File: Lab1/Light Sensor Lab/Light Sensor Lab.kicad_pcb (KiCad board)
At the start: 2 copper layers, 19.3 x 19.8 mm, 9 parts, among them J1 Conn_01x03, U1 LMC6482

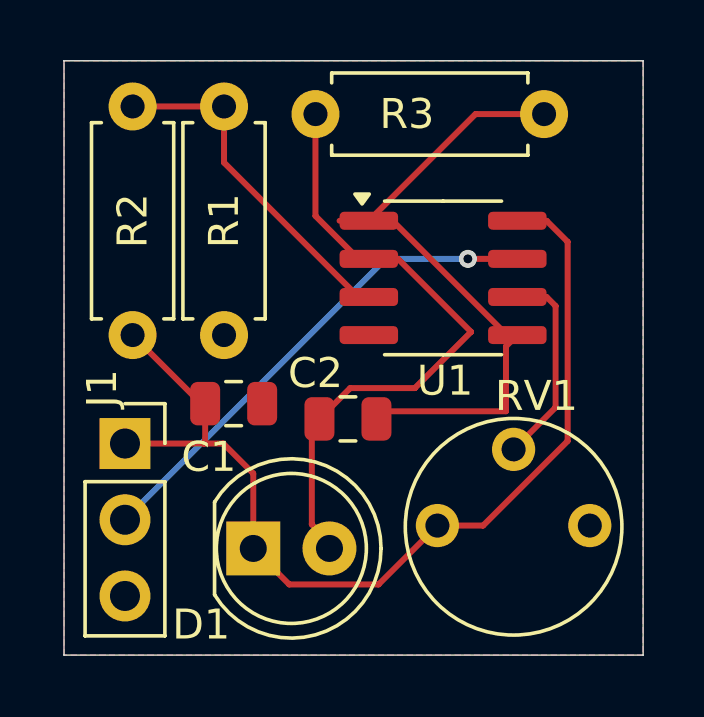
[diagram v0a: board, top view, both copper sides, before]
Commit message: small trace tweeks
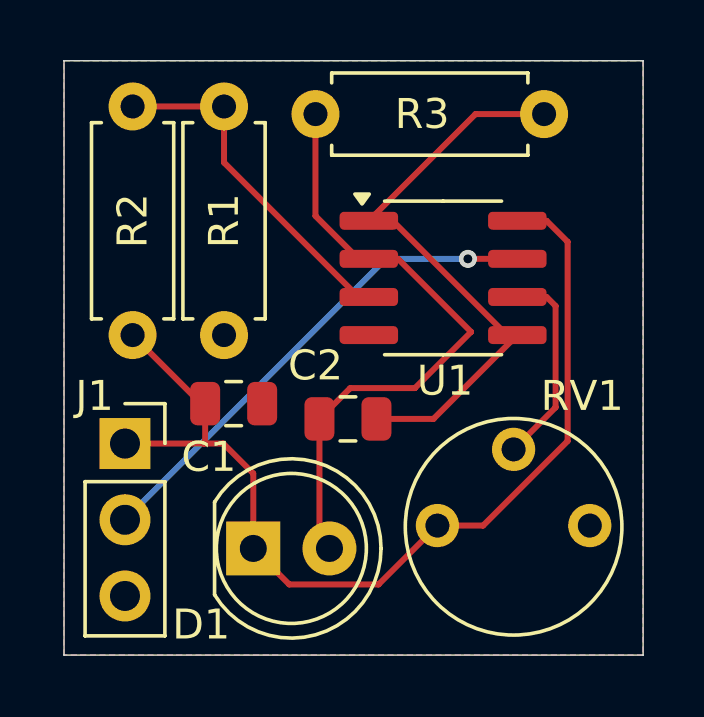
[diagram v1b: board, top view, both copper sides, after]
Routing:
- net Net-(U1B-+): track 22.1 -> 19.7 mm
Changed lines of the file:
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@@
 		(tags "capacitor")
 		(property "Reference" "C2"
-			(at -1.082 -1.524 0)
+			(at -1.082 -1.778 0)
 			(layer "F.SilkS")
 			(effects
@@
 		(tags "Resistor Axial_DIN0207 series Axial Horizontal pin pitch 7.62mm 0.25W = 1/4W length 6.3mm diameter 2.5mm")
 		(property "Reference" "R3"
-			(at 3.048 0 0)
+			(at 3.556 0 0)
 			(layer "F.SilkS")
 			(effects
@@
 		(tags "Through hole socket strip THT 1x03 2.54mm single row")
 		(property "Reference" "J1"
-			(at -0.762 -1.838 90)
+			(at -1.016 -1.584 180)
 			(layer "F.SilkS")
 			(effects
@@
 		(tags "Potentiometer vertical Vishay T7-YA Single")
 		(property "Reference" "RV1"
-			(at 4.318 -1.778 180)
+			(at 4.318 -0.254 180)
 			(layer "F.SilkS")
 			(effects
@@
 		(layer "Edge.Cuts")
 	)
+	(dimension
+		(type orthogonal)
+		(layer "F.Cu")
+		(pts
+			(xy 158.496 78.74) (xy 139.192 78.74)
+		)
+		(height -3.048)
+		(orientation 0)
+		(format
+			(prefix "")
+			(suffix "")
+			(units 3)
+			(units_format 0)
+			(precision 4)
+			(suppress_zeroes yes)
+		)
+		(style
+			(thickness 0.2)
+			(arrow_length 1.27)
+			(text_position_mode 0)
+			(arrow_direction outward)
+			(extension_height 0.58642)
+			(extension_offset 0.5)
+			(keep_text_aligned yes)
+		)
+		(gr_text "19.304"
+			(at 148.844 73.892 0)
+			(layer "F.Cu")
+			(effects
+				(font
+					(size 1.5 1.5)
+					(thickness 0.3)
+				)
+			)
+		)
+	)
+	(dimension
+		(type orthogonal)
+		(layer "F.Cu")
+		(pts
+			(xy 158.496 98.552) (xy 158.496 78.74)
+		)
+		(height 5.08)
+		(orientation 1)
+		(format
+			(prefix "")
+			(suffix "")
+			(units 3)
+			(units_format 0)
+			(precision 4)
+			(suppress_zeroes yes)
+		)
+		(style
+			(thickness 0.2)
+			(arrow_length 1.27)
+			(text_position_mode 0)
+			(arrow_direction outward)
+			(extension_height 0.58642)
+			(extension_offset 0.5)
+			(keep_text_aligned yes)
+		)
+		(gr_text "19.812"
+			(at 161.776 88.646 90)
+			(layer "F.Cu")
+			(effects
+				(font
+					(size 1.5 1.5)
+					(thickness 0.3)
+				)
+			)
+		)
+	)
 	(segment
 		(start 141.478 87.884)
@@
 	)
 	(segment
-		(start 148.04 94.996)
-		(end 148.04 94.784)
+		(start 147.706 94.662)
+		(end 148.04 94.996)
+		(width 0.2)
+		(layer "F.Cu")
+		(net 3)
+	)
+	(segment
+		(start 147.706 90.678)
+		(end 147.706 94.662)
 		(width 0.2)
 		(layer "F.Cu")
@@
 	)
 	(segment
-		(start 147.452 94.196)
-		(end 147.452 90.424)
-		(width 0.2)
-		(layer "F.Cu")
-		(net 3)
-	)
-	(segment
 		(start 150.886001 89.652)
 		(end 148.732 89.652)
@@
 	)
 	(segment
-		(start 148.04 94.784)
-		(end 147.452 94.196)
-		(width 0.2)
-		(layer "F.Cu")
-		(net 3)
-	)
-	(segment
 		(start 155.194 80.518)
 		(end 152.908 80.518)
@@
 	)
 	(segment
-		(start 154.302 87.884)
-		(end 153.924 88.262)
-		(width 0.2)
-		(layer "F.Cu")
-		(net 4)
-	)
-	(segment
-		(start 153.924 90.424)
-		(end 149.352 90.424)
-		(width 0.2)
-		(layer "F.Cu")
-		(net 4)
-	)
-	(segment
 		(start 149.352 84.074)
 		(end 150.145032 84.074)
@@
 	)
 	(segment
+		(start 151.508 90.678)
+		(end 154.302 87.884)
+		(width 0.2)
+		(layer "F.Cu")
+		(net 4)
+	)
+	(segment
+		(start 149.606 90.678)
+		(end 151.508 90.678)
+		(width 0.2)
+		(layer "F.Cu")
+		(net 4)
+	)
+	(segment
 		(start 153.955032 87.884)
 		(end 154.302 87.884)
@@
 		(width 0.2)
 		(layer "F.Cu")
-		(net 4)
-	)
-	(segment
-		(start 148.377001 84.074)
-		(end 149.352 84.074)
-		(width 0.2)
-		(layer "F.Cu")
-		(net 4)
-	)
-	(segment
-		(start 153.924 88.262)
-		(end 153.924 90.424)
-		(width 0.2)
-		(layer "F.Cu")

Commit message: Made light sensor slightly smaller
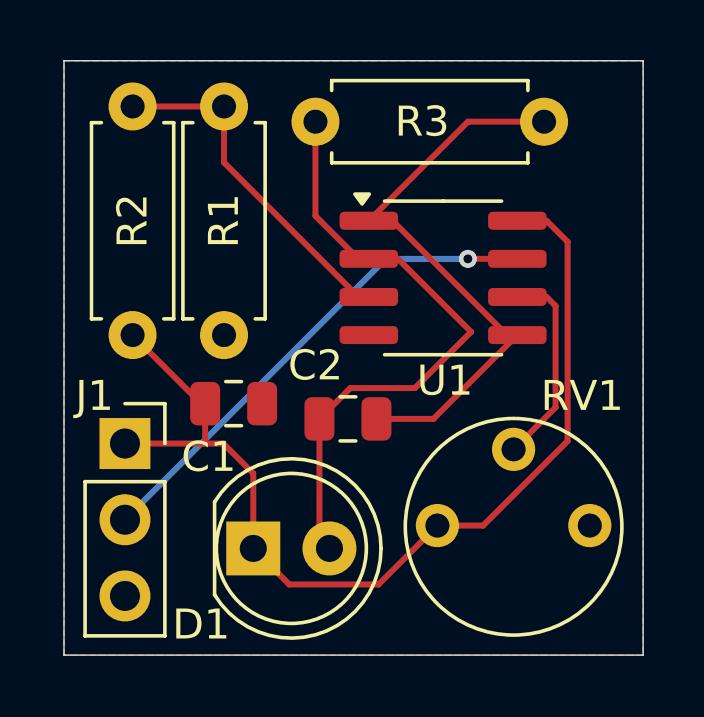
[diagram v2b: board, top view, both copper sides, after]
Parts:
- moved R3 0.25 mm to (147.6, 80.8)
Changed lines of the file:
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@@
 	(footprint "Resistor_THT:R_Axial_DIN0207_L6.3mm_D2.5mm_P7.62mm_Horizontal"
 		(layer "F.Cu")
-		(at 147.574 80.518)
+		(at 147.574 80.772)
 		(descr "Resistor, Axial_DIN0207 series, Axial, Horizontal, pin pitch=7.62mm, 0.25W = 1/4W, length*diameter=6.3*2.5mm^2, http://cdn-reichelt.de/documents/datenblatt/B400/1_4W%23YAG.pdf")
 		(tags "Resistor Axial_DIN0207 series Axial Horizontal pin pitch 7.62mm 0.25W = 1/4W length 6.3mm diameter 2.5mm")
@@
 	)
 	(segment
+		(start 147.574 83.912968)
+		(end 149.005032 85.344)
+		(width 0.2)
+		(layer "F.Cu")
+		(net 3)
+	)
+	(segment
 		(start 147.706 90.678)
 		(end 147.706 94.662)
@@
 	)
 	(segment
+		(start 149.005032 85.344)
+		(end 149.352 85.344)
+		(width 0.2)
+		(layer "F.Cu")
+		(net 3)
+	)
+	(segment
 		(start 152.7605 87.777501)
 		(end 150.326999 85.344)
@@
 	)
 	(segment
-		(start 147.574 83.912968)
-		(end 149.005032 85.344)
-		(width 0.2)
-		(layer "F.Cu")
-		(net 3)
-	)
-	(segment
 		(start 152.7605 87.777501)
 		(end 150.886001 89.652)
@@
 	)
 	(segment
-		(start 147.574 80.518)
+		(start 147.574 80.772)
 		(end 147.574 83.912968)
 		(width 0.2)
@@
 	)
 	(segment
-		(start 149.005032 85.344)
-		(end 149.352 85.344)
-		(width 0.2)
-		(layer "F.Cu")
-		(net 3)
-	)
-	(segment
-		(start 155.194 80.518)
-		(end 152.908 80.518)
-		(width 0.2)
-		(layer "F.Cu")
-		(net 4)
-	)
-	(segment
-		(start 152.908 80.518)
-		(end 149.352 84.074)
+		(start 155.194 80.772)
+		(end 152.654 80.772)
 		(width 0.2)
 		(layer "F.Cu")
@@
 		(width 0.2)
 		(layer "F.Cu")
+		(net 4)
+	)
+	(segment
+		(start 152.654 80.772)
+		(end 149.352 84.074)
+		(width 0.2)
+		(layer "F.Cu")
